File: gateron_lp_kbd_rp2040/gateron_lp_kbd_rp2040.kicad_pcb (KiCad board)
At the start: 4 copper layers, 234.5 x 116.5 mm, 306 parts, among them J1 TYPE-C-31-M-12, J2 Battery JST-SH, Q1 DMG3415U, SW1 KS-33, SW10 KS-33, SW11 KS-33, SW12 KS-33, SW13 KS-33, SW14 KS-33, SW15 KS-33, SW16 KS-33, SW17 KS-33, SW18 KS-33, SW19 KS-33, SW2 KS-33, SW20 KS-33, SW21 KS-33, SW22 KS-33, SW23 KS-33, SW24 KS-33, SW25 KS-33, SW26 KS-33, SW27 KS-33, SW28 KS-33, SW29 KS-33, SW3 KS-33, SW30 KS-33, SW31 KS-33, SW32 KS-33, SW33 KS-33, SW34 KS-33, SW35 KS-33, SW36 KS-33, SW37 KS-33, SW38 KS-33, SW39 KS-33, SW4 KS-33, SW40 KS-33, SW41 KS-33, SW42 KS-33, SW43 KS-33, SW44 KS-33, SW45 KS-33, SW46 KS-33, SW47 KS-33, SW48 KS-33, SW49 KS-33, SW5 KS-33, SW50 KS-33, SW51 KS-33, SW52 KS-33, SW53 KS-33, SW54 KS-33, SW55 KS-33, SW56 KS-33, SW57 KS-33, SW58 KS-33, SW59 KS-33, SW6 KS-33, SW60 RESET, SW61 BOOTSEL, SW62 PWR MSK-12C02, SW7 KS-33, SW8 KS-33, SW9 KS-33, U1 RP2040, U2 MCP73831, U3 AP2112K-3.3, U4 USBLC6-2SC6, U5 W25Q16JVUXIQ, U6 CYW43439, U7 SN74AHCT1G125DBVR, Y1 12MHz, Y2 37.4MHz

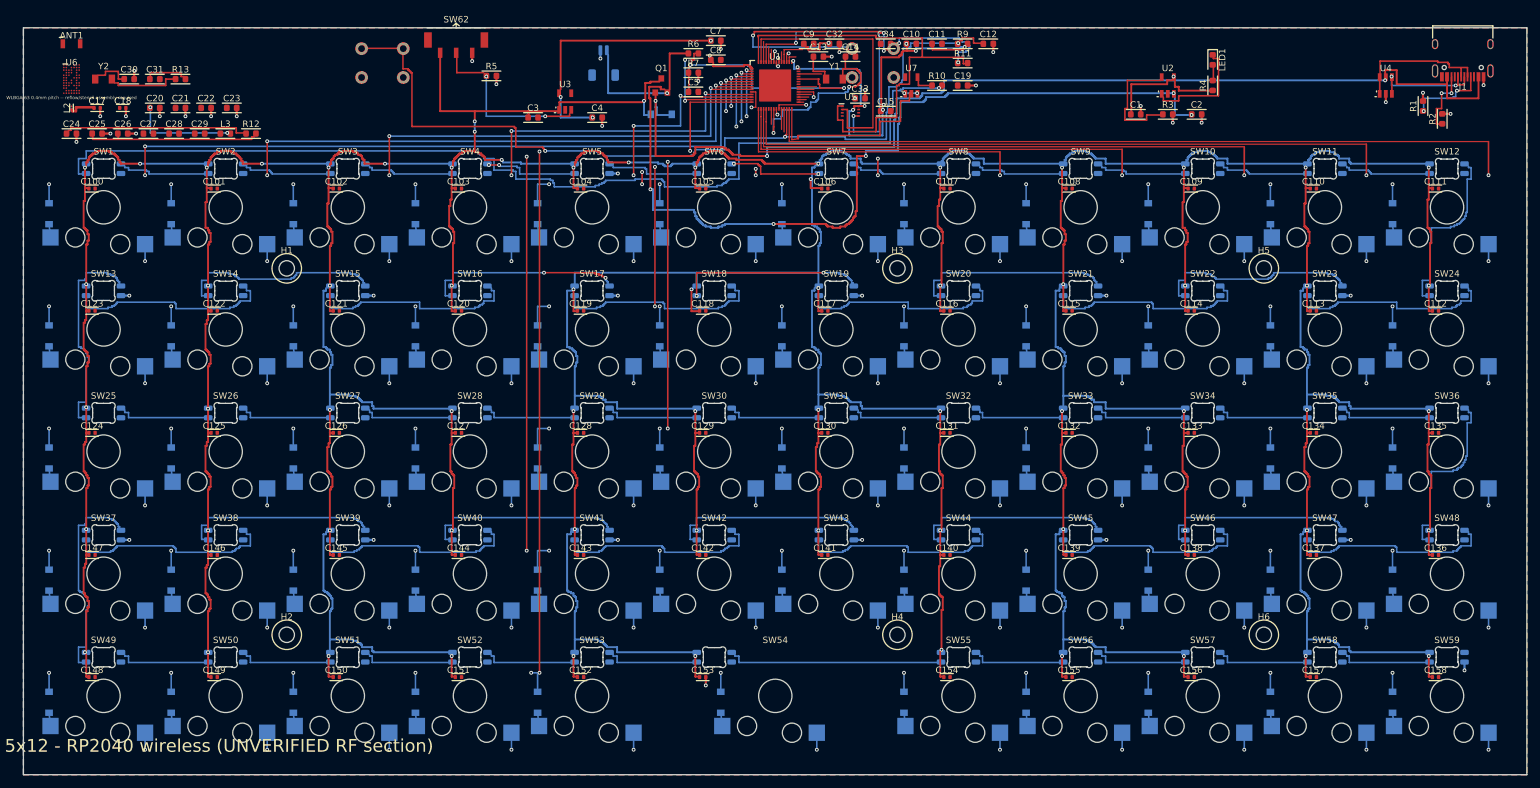
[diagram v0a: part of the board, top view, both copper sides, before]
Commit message: Fix 3 drilled shorts, 59 switch collisions + hole violations; add fiducials
Four manufacturability fixes found by the (now 4-layer) drc_check plus
the KS-33 vendor STEP model, all applied in the generator and verified
by a full regenerate -> route -> DRC cycle:

- SW61 (BOOTSEL) moved (170,27.5) -> (196,27.5): its THT pads sat at
  0.000mm from Y1.2 (XOUT), C14.1 and C34.2 -- three drilled shorts.
  Its four through-holes were also the 'BOOTSEL keepout' wall the
  router kept fighting in the U1-north escape pocket. New spot is the
  verified-empty band between C12/R11 and C1/U2.
- Per-LED 100nF caps (C100-C158) moved to B.Cu and nudged 3.1 -> 3.0mm:
  the KS-33's bottom housing is flush at z=0 over the old F.Cu spot
  (checked the vendor STEP point cloud), so a top-side 0402 kept every
  switch from seating. Same XY on B keeps hole clearances by symmetry
  and puts the cap on the same layer as the reverse-mount LED it
  decouples. The 0.1mm nudge fixes 59x 0.207mm hole-to-copper
  violations against the 5.2mm stem NPTH (now 0.30mm >= the 0.25 rule).
- 3 fiducials per side (1mm dot, 2mm mask opening), asymmetric triangle,
  clear of the antenna keepout -- required for 0.4mm-pitch QFN/BGA
  assembly with SMD on both sides.
- D60's PCB value fixed 1N4148W -> B5819W so a PCB-side BOM can't stuff
  a 150mA signal diode into the VBUS power path.

DRC after: 0 hole, 0 edge violations; the only sub-0.19mm items left are
3 track clearances (0.125-0.174mm, fab-legal) and the QFN-56/WLBGA-63
packages' own 0.15mm pad gaps. Split nets unchanged (the known QSPI
pocket + U6 BGA stubs).

Co-Authored-By: Claude Fable 5 <noreply@anthropic.com>
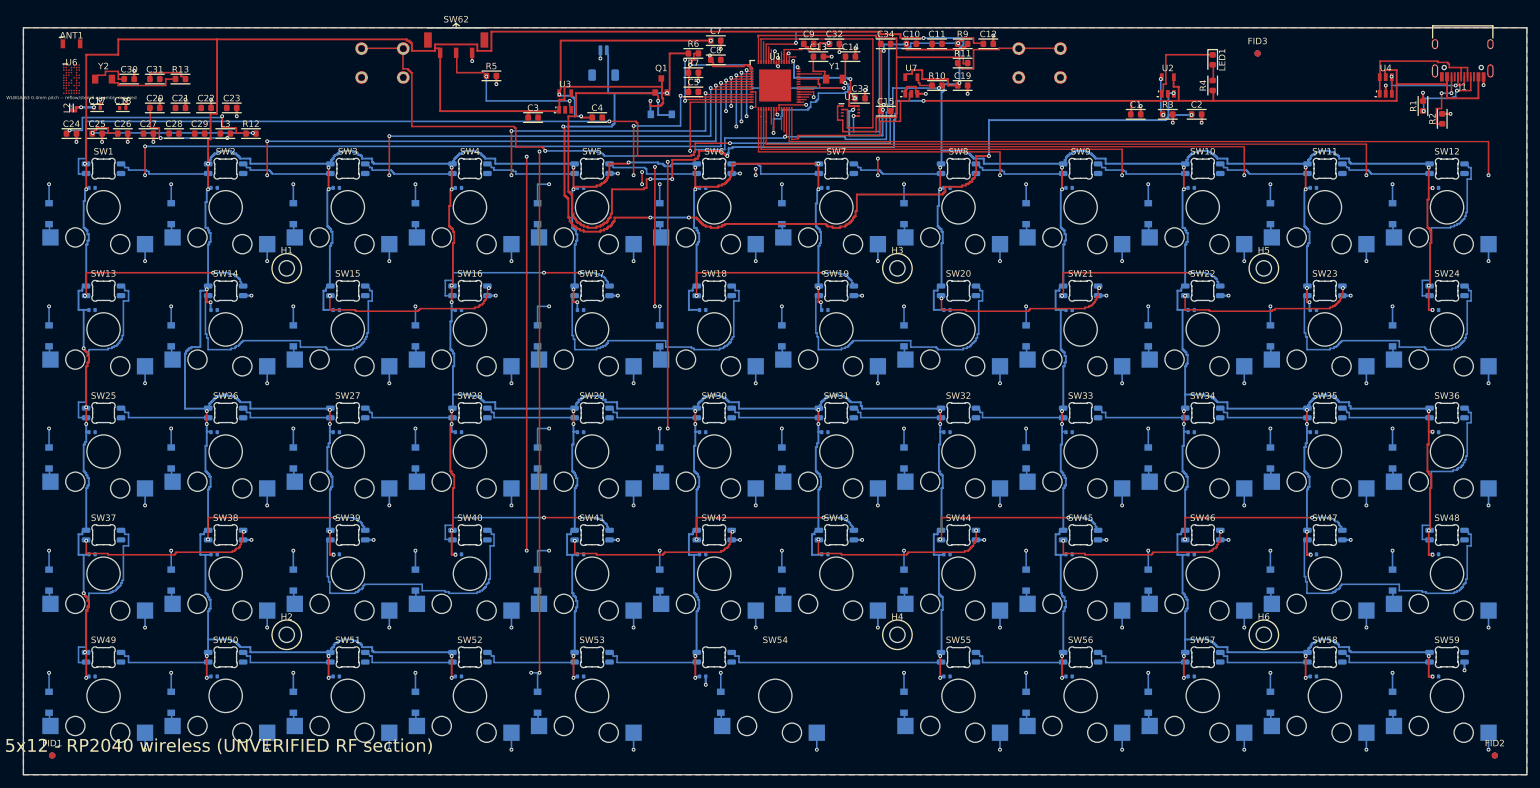
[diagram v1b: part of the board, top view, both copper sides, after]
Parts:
- added FID1: FIDUCIAL, kbd:FIDUCIAL_1MM, F.Cu at (42.0, 135.5)
- added FID2: FIDUCIAL, kbd:FIDUCIAL_1MM, F.Cu at (267.0, 135.5)
- added FID3: FIDUCIAL, kbd:FIDUCIAL_1MM, F.Cu at (230.0, 26.0)
- added FID4: FIDUCIAL, kbd:FIDUCIAL_1MM, B.Cu at (42.0, 135.5)
- added FID5: FIDUCIAL, kbd:FIDUCIAL_1MM, B.Cu at (267.0, 135.5)
- added FID6: FIDUCIAL, kbd:FIDUCIAL_1MM, B.Cu at (230.0, 26.0)
- C100, C101, C102, C103, C104, C105, C106, C107, C108, C109, C110, C111, C112, C113, C114, C115, C116, C117, C118, C119, C120, C121, C122, C123, C124, C125, C126, C127, C128, C129, C130, C131, C132, C133, C134, C135, C136, C137, C138, C139, C140, C141, C142, C143, C144, C145, C146, C147, C148, C149, C150, C151, C152, C153, C154, C155, C156, C157, C158: moved to B.Cu
- D60: value 1N4148W -> B5819W
- moved SW61 26.0 mm to (196.0, 27.5)
- moved C148 0.10 mm to (48.2, 123.2)
- moved C149 0.10 mm to (67.2, 123.2)
- moved C150 0.10 mm to (86.3, 123.2)
- moved C151 0.10 mm to (105.3, 123.2)
- moved C152 0.10 mm to (124.4, 123.2)
- moved C153 0.10 mm to (143.4, 123.2)
- moved C154 0.10 mm to (181.6, 123.2)
- moved C155 0.10 mm to (200.6, 123.2)
- moved C156 0.10 mm to (219.7, 123.2)
- moved C157 0.10 mm to (238.7, 123.2)
- moved C158 0.10 mm to (257.8, 123.2)
- moved C100 0.10 mm to (48.2, 47.0)
- moved C101 0.10 mm to (67.2, 47.0)
- moved C102 0.10 mm to (86.3, 47.0)
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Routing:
- net VSYS: track 1445.3 -> 1606.3 mm, vias 68 -> 96
- net BOOTSEL: track 61.9 -> 19.5 mm, vias 5 -> 0
- net VBUS: track 186.7 -> 225.1 mm, vias 4 -> 5
- net BAT+: track 158.8 -> 178.6 mm, vias 6 -> 7
- net LEDD19: track 33.4 -> 47.8 mm
- net LEDD17: track 33.3 -> 47.7 mm
- net LEDD45: track 33.3 -> 47.7 mm
- net LEDD37: track 33.3 -> 47.7 mm
- net LEDD13: track 33.3 -> 47.7 mm
- net LEDD22: track 33.8 -> 47.6 mm
- net PROG: track 18.7 -> 6.13 mm, vias 0 -> 2
- net GND: track 58.0 -> 68.5 mm, vias 45 -> 50
- net XOUT: track 34.0 -> 28.2 mm
- net +3V3: track 223.4 -> 217.8 mm, vias 18 -> 17
- net LEDD24: track 35.2 -> 29.8 mm
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
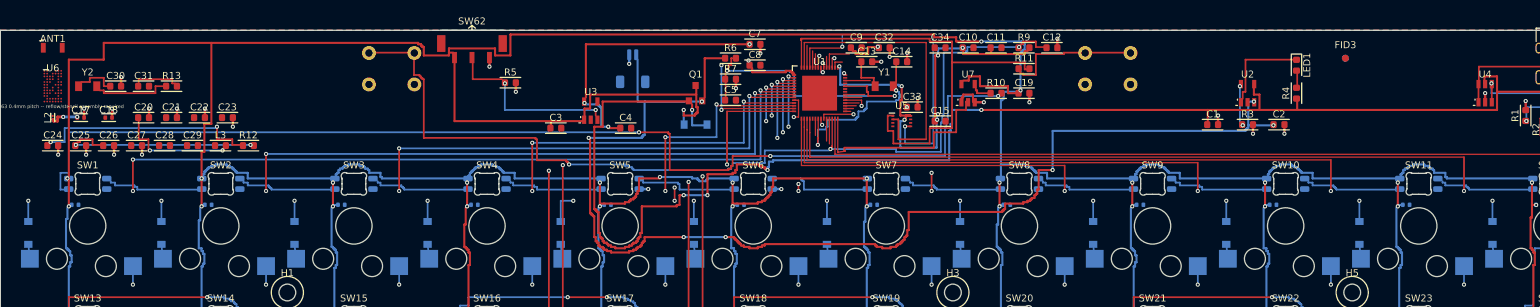
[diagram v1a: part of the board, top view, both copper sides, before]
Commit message: Relocate U5 flash beside the QSPI bank; route all 7 stuck nets + RF feed
The QSPI flash sat SOUTH-EAST of U1 while the QSPI pins exit NORTH, so
every QSPI line wrapped around U1's east side. The lane/elevator system
that required (QSPI_SD1's F lane at y=23.75 spanning x 152.55-170, plus
the x=170-174 elevators) sealed the whole U1-north pocket -- QSPI_SD2/
SCLK/SD3, XIN, VREG_VIN and USB_DM/DP were all unroutable behind it,
which is what the last ~10 commits kept hitting from different angles.

U5 now sits at (149.8, 24.0), directly west of the QSPI pin bank (the
Pico reference design's arrangement), with C15 (its VCC cap, now 0402)
alongside. QSPI escape stubs get hand-picked depths instead of the
uniform staircase: SD3/SCLK/SD0's tips land exactly on U5's east-column
pad rows (three dead-straight lanes), SS/SD1/SD2 wrap U5's south-west
corner into the west column -- all emitted as must_clear_seg-verified
deterministic copper. The old lane/elevator code and the forced skips
for QSPI_SD2/SCLK/SD3 are deleted.

Knock-on fixes, each found by the emit-time clearance assertions:
- claim-order restructure: USB_DM's jogs, then v43/v48/v49 (2mm search
  radius, most fragile), then the DVDD pin-45/50 via gather, then
  VREG_VIN's jog -- all before the minimum-system A* nets are free to
  claim the reopened pocket's corridors
- XIN routes before XOUT (and C13-first): XIN's escape tip sits one
  pin-pitch inside XOUT's, so whichever routes first claims the only
  southern corridor; XOUT's east-pad target is the easier second
- +3V3 pin 33's In1 expressway retargeted to C11's pad (its old landing
  spot was C15's now-vacated position), passing south of DVDD's riser
- QSPI_SS's redundant second chain removed (the SW wrap already ties
  U5.1 to the stub)
- WLRF_ANT_MID feed is deterministic 0.4mm RF copper: generic A* can
  never route it (the mask bans the whole antenna keepout, and a 0.4mm
  trace can only attach to L2's 0201 pad at its outer edge). Riser at
  x=47.5 between U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
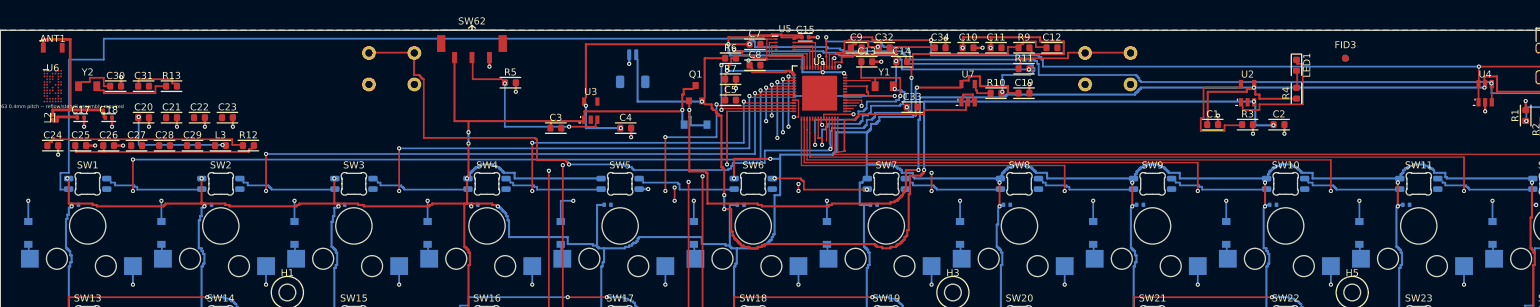
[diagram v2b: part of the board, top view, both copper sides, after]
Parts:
- C15: footprint kbd:RC_0603 -> kbd:RC_0402
- moved C15 22.7 mm to (152.7, 23.0)
- moved U5 20.0 mm to (149.8, 24.0)
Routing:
- net USB_DP: track 19.6 -> 123.9 mm, vias 2 -> 3
- net VSYS: track 1606.3 -> 1502.9 mm, vias 96 -> 93
- net USB_DM: track 27.4 -> 125.8 mm, vias 0 -> 2
- net QSPI_SD0: track 45.3 -> 4.88 mm, vias 2 -> 0
- net QSPI_SD1: track 42.5 -> 9.57 mm
- net VBUS: track 225.1 -> 193.9 mm, vias 5 -> 4
- net XIN: track 7.30 -> 35.0 mm, vias 0 -> 2
- net BAT+: track 178.6 -> 151.4 mm, vias 7 -> 6
- net WLRF_ANT_MID: track 0.00 -> 24.2 mm
- net +3V3: track 217.8 -> 240.4 mm, vias 17 -> 14
- net VREG_VIN: track 1.85 -> 17.7 mm
- net LEDD0_R: track 159.9 -> 174.5 mm, vias 3 -> 1
- net PROG: track 6.13 -> 18.7 mm, vias 2 -> 0
- net QSPI_SD2: track 3.20 -> 8.77 mm
- net QSPI_SS: track 67.1 -> 61.7 mm, vias 0 -> 2
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
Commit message: BOM: key positions are the hot-swap socket, not the switch
The soldered part at each key position is the Gateron KS-2P02B01-02
hot-swap socket -- the KS-33 switch (and keycap) plug in and are
user-installed, ordered from keyboard vendors rather than with the PCB
parts. The BOM previously listed 59x "KS-33" (58 + one "2U") and no
socket at all, so nothing reminded anyone to order the one part that
actually gets reflowed.

- sym_inst() grows a props= param for extra hidden symbol properties
- SW1-59 now carry Value/MPN "KS-2P02B01-02", Manufacturer "Gateron",
  and a BOM Comment noting the switch/keycap are separate purchases
  (plus a 2U keycap/stabilizer note on SW54)
- footprint Value matches, keeping sch/PCB cross-checks clean
- BOM collapses to one clean 59x socket line (43 lines total)

Note: the footprint still has exclude_from_pos_files (inherited from
when it modeled the switch) -- if the sockets are ever machine-placed
by an assembly service, that flag needs to go.

Co-Authored-By: Claude Fable 5 <noreply@anthropic.com>
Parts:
- SW1, SW10, SW11, SW12, SW13, SW14, SW15, SW16, SW17, SW18, SW19, SW2, SW20, SW21, SW22, SW23, SW24, SW25, SW26, SW27, SW28, SW29, SW3, SW30, SW31, SW32, SW33, SW34, SW35, SW36, SW37, SW38, SW39, SW4, SW40, SW41, SW42, SW43, SW44, SW45, SW46, SW47, SW48, SW49, SW5, SW50, SW51, SW52, SW53, SW54, SW55, SW56, SW57, SW58, SW59, SW6, SW7, SW8, SW9: value KS-33 -> KS-2P02B01-02
